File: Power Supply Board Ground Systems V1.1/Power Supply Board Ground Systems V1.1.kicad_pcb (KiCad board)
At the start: 2 copper layers, 76.2 x 38.1 mm, 32 parts, among them J1 POWER, J2 POWER OUT, SW1 SW_SPDT, SW2 SW_SPDT, SW3 SW_SPDT, SW4 SW_SPDT, SW5 SW_SPDT, SW6 SW_SPDT, SW7 SW_SPDT, SW8 SW_SPDT

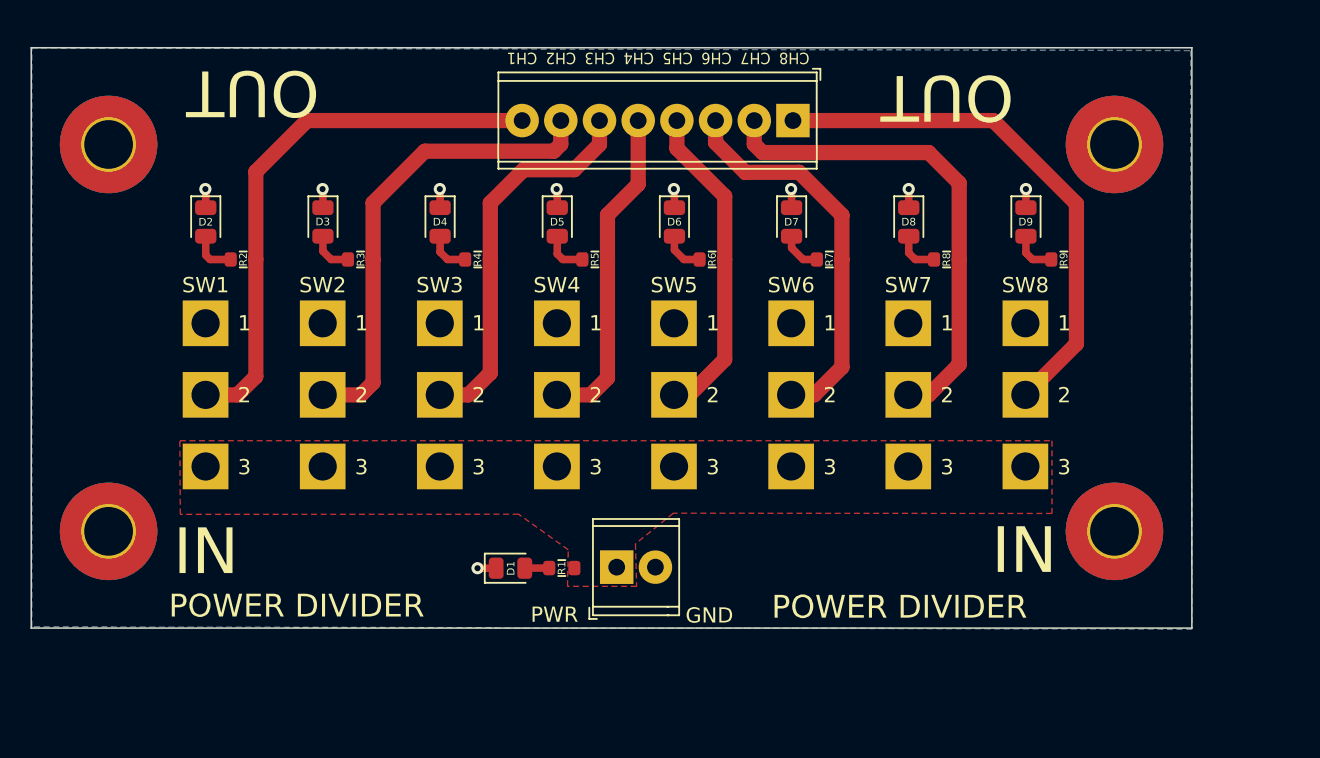
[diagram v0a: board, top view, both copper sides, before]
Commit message: Changed all the things to 5mm pitch
yuck big board be like
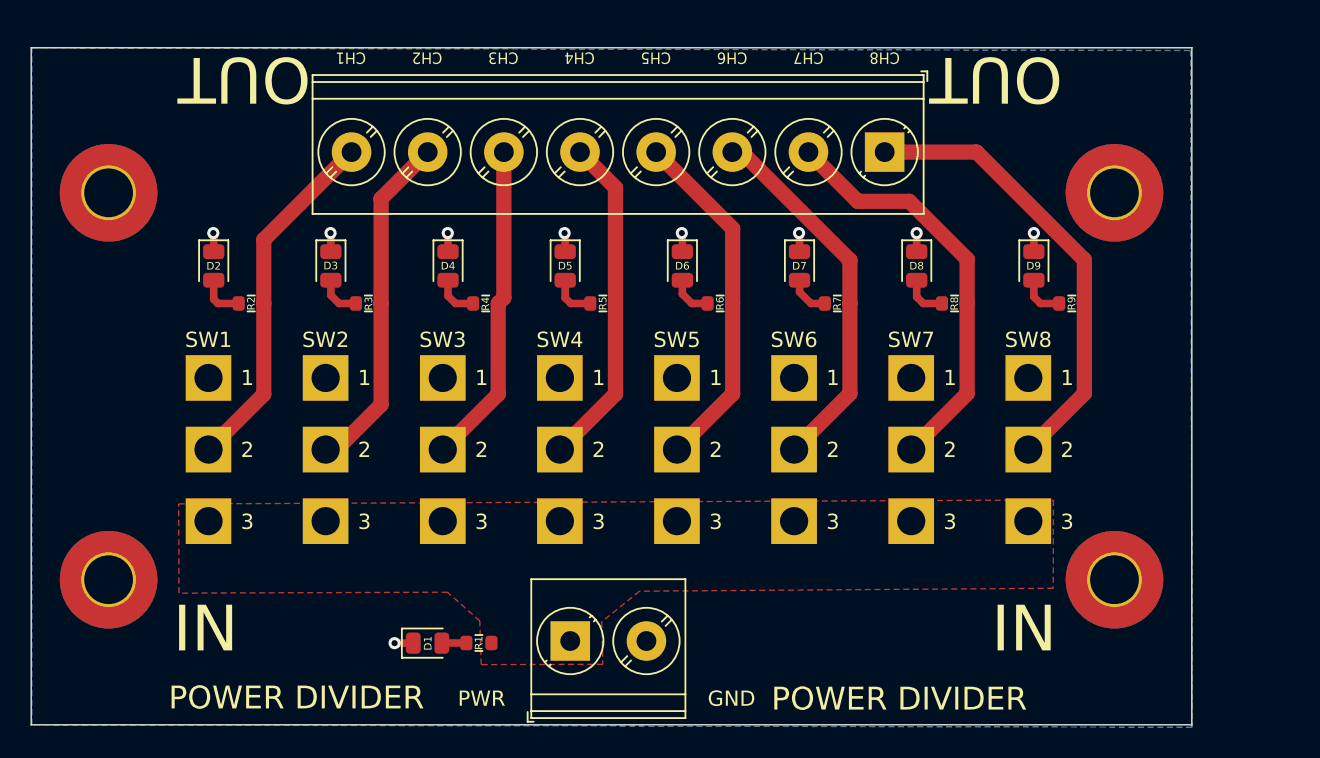
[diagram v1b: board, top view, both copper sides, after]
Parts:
- J1: footprint TerminalBlock_Phoenix:TerminalBlock_Phoenix_MPT-0,5-2-2.54_1x02_P2.54mm_Horizontal -> TerminalBlock_Phoenix:TerminalBlock_Phoenix_PT-1,5-2-5.0-H_1x02_P5.00mm_Horizontal
- J2: footprint TerminalBlock_Phoenix:TerminalBlock_Phoenix_MPT-0,5-8-2.54_1x08_P2.54mm_Horizontal -> TerminalBlock_Phoenix:TerminalBlock_Phoenix_PT-1,5-8-5.0-H_1x08_P5.00mm_Horizontal
- moved D1 7.34 mm to (51.4, 64.5)
- moved R1 7.34 mm to (54.8, 64.5)
- moved J2 6.37 mm to (81.4, 32.2)
- moved J1 5.73 mm to (60.8, 64.3)
- moved SW1 3.60 mm to (37.0, 47.1)
- moved SW2 3.60 mm to (44.7, 47.1)
- moved SW3 3.60 mm to (52.4, 47.1)
- moved SW4 3.60 mm to (60.1, 47.1)
- moved SW5 3.60 mm to (67.8, 47.1)
- moved SW6 3.60 mm to (75.5, 47.1)
- moved SW7 3.60 mm to (83.2, 47.1)
- moved SW8 3.60 mm to (90.9, 47.1)
- moved H2 3.18 mm to (30.5, 60.3)
- moved H4 3.18 mm to (96.5, 60.3)
- moved H1 3.17 mm to (30.5, 34.9)
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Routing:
- net OUT1: track 36.1 -> 23.4 mm
- net OUT2: track 30.9 -> 22.7 mm
- net OUT7: track 32.1 -> 27.4 mm
- net OUT8: track 34.8 -> 30.0 mm
- net OUT3: track 25.4 -> 21.2 mm
- net OUT5: track 21.3 -> 23.1 mm
- net OUT6: track 25.8 -> 24.6 mm
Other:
- board size 76.2 x 38.1 mm -> 76.2 x 44.4 mm

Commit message: Lots of schematic changes
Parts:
- moved H3 6.35 mm to (102.9, 34.9)
- moved H4 6.35 mm to (102.9, 60.3)
- moved R4 2.62 mm to (57.8, 42.4)
- moved D2 2.62 mm to (40.0, 40.0)
- moved D3 2.62 mm to (47.7, 40.0)
- moved D4 2.62 mm to (55.4, 40.0)
- moved D5 2.62 mm to (63.1, 40.0)
- moved D6 2.62 mm to (70.8, 40.0)
- moved D7 2.62 mm to (78.5, 40.0)
- moved D8 2.62 mm to (86.1, 40.0)
- moved D9 2.62 mm to (93.8, 40.0)
- moved R2 2.62 mm to (42.5, 42.4)
- moved R3 2.62 mm to (50.1, 42.4)
- moved R5 2.62 mm to (65.5, 42.4)
- moved R6 2.62 mm to (73.2, 42.4)
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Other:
- board size 76.2 x 44.4 mm -> 82.6 x 44.4 mm

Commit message: Revions and new board
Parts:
- removed J1: POWER, TerminalBlock_Phoenix:TerminalBlock_Phoenix_PT-1,5-2-5.0-H_1x02_P5.00mm_Horizontal
- removed J2: POWER OUT, TerminalBlock_Phoenix:TerminalBlock_Phoenix_PT-1,5-8-5.0-H_1x08_P5.00mm_Horizontal
- added J3: TBLH10V-350-02BK, TBLH10V-350-02BK:RHDR4W80P550X350_2X2_770X850X1420P, F.Cu at (62.6, 68.3)
- added J4: TBLH10V-350-08BK, TBLH10V-350-08BK:RHDR16W80P550X350_2X8_2870X850X1420P, F.Cu at (53.2, 33.2)
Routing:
- net OUT8: track 29.6 -> 41.2 mm
- net OUT7: track 27.0 -> 37.2 mm
- net OUT1: track 23.0 -> 31.8 mm
- net OUT6: track 24.2 -> 32.9 mm
- net OUT5: track 22.7 -> 30.0 mm
- net OUT2: track 22.6 -> 28.5 mm
- net OUT3: track 20.8 -> 26.1 mm
- net OUT4: track 21.6 -> 26.6 mm

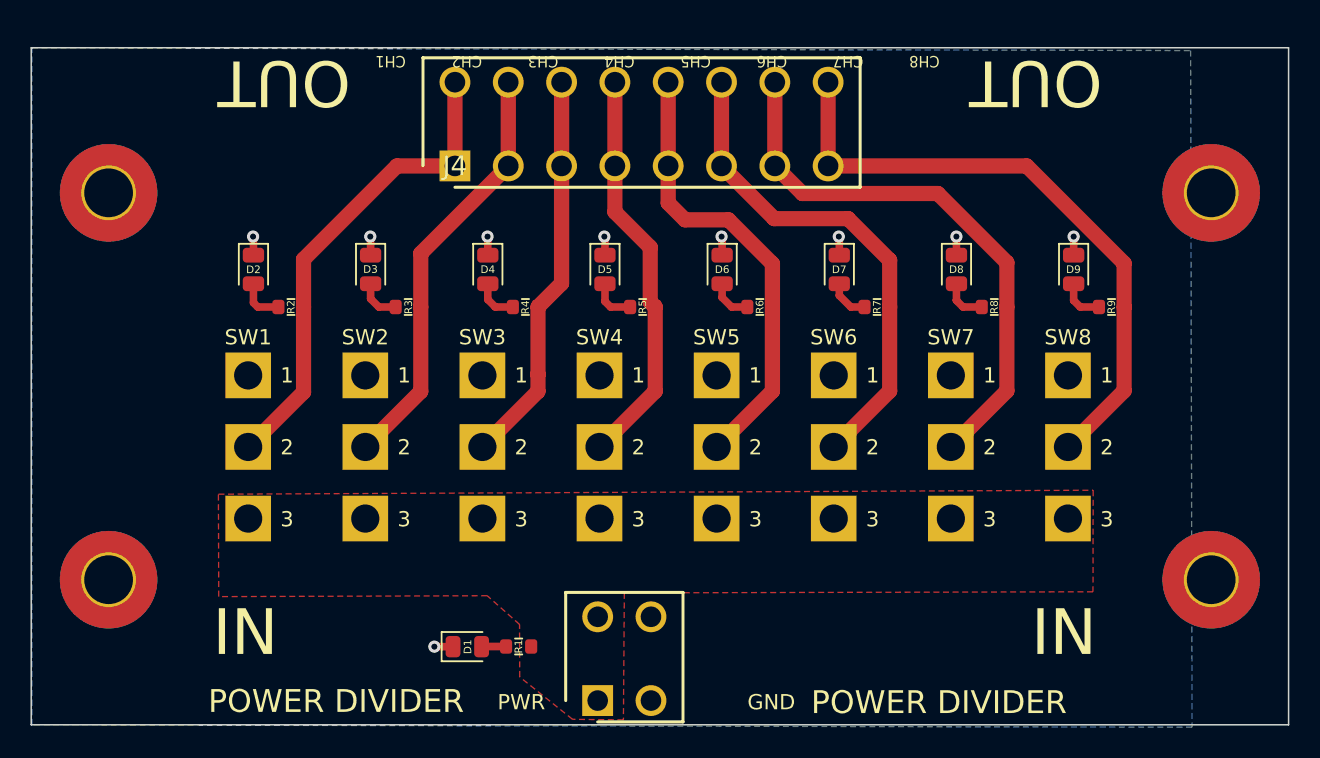
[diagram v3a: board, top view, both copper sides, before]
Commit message: Added BOMS
https://www.digikey.com/short/8btm0n25
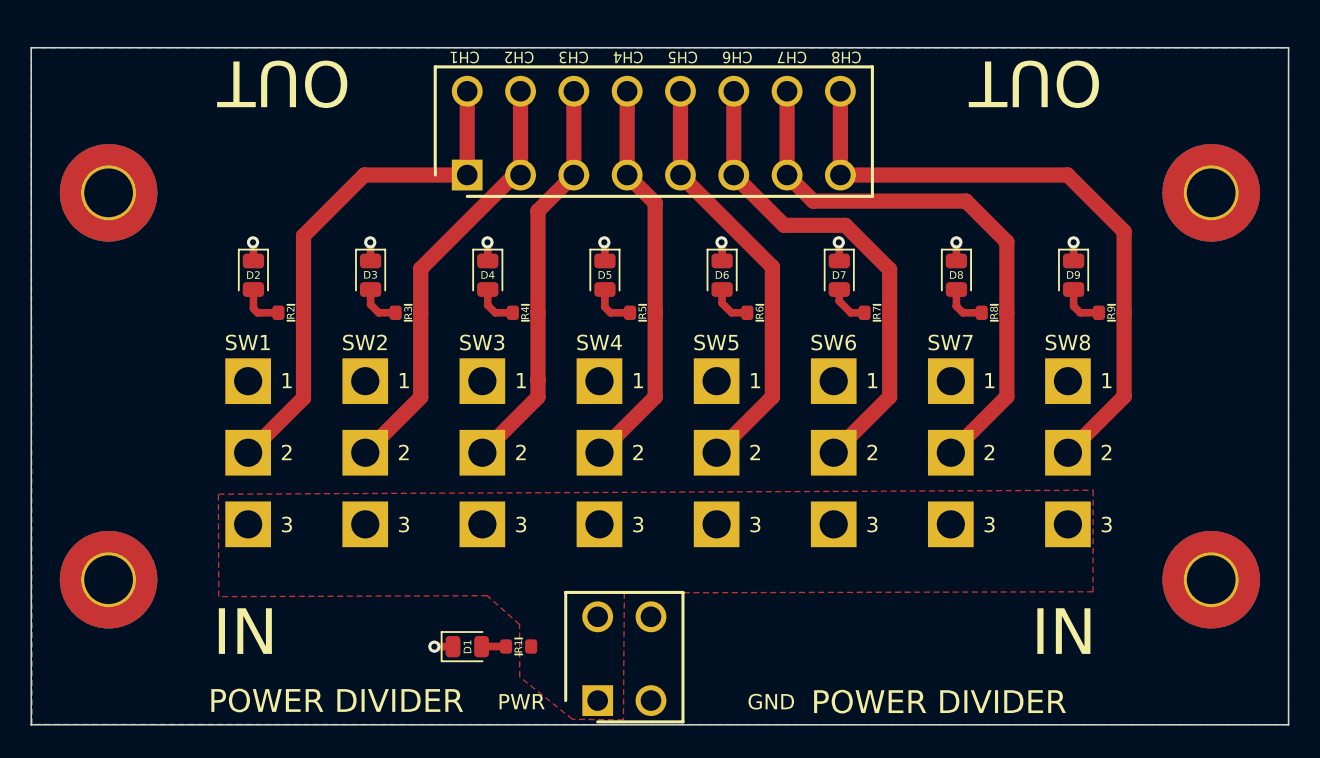
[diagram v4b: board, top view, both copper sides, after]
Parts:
- moved J4 1.00 mm to (54.0, 33.8)
- moved SW1 0.38 mm to (39.6, 47.3)
- moved SW2 0.38 mm to (47.3, 47.3)
- moved SW3 0.38 mm to (55.0, 47.3)
- moved SW4 0.38 mm to (62.7, 47.3)
- moved SW5 0.38 mm to (70.4, 47.3)
- moved SW6 0.38 mm to (78.1, 47.3)
- moved SW7 0.38 mm to (85.8, 47.3)
- moved SW8 0.38 mm to (93.5, 47.3)
- moved D2 0.38 mm to (40.0, 40.3)
- moved D3 0.38 mm to (47.7, 40.3)
- moved D4 0.38 mm to (55.4, 40.3)
- moved D5 0.38 mm to (63.1, 40.3)
- moved D6 0.38 mm to (70.8, 40.3)
- moved D7 0.38 mm to (78.5, 40.3)
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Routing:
- net OUT5: track 30.0 -> 27.8 mm
- net OUT1: track 31.8 -> 33.7 mm
- net OUT6: track 32.9 -> 31.9 mm
- net OUT8: track 41.2 -> 41.7 mm
- net OUT4: track 26.6 -> 26.0 mm
